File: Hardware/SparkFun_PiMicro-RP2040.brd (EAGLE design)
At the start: 17.8 x 33 mm, 105 parts, among them J2 Qwiic, J5 USB Female Type C Connector, U1 3.3V, U2 RP2040, U3 WS2812-2020, U4 W25QXX128MBIT, Y1 12MHz

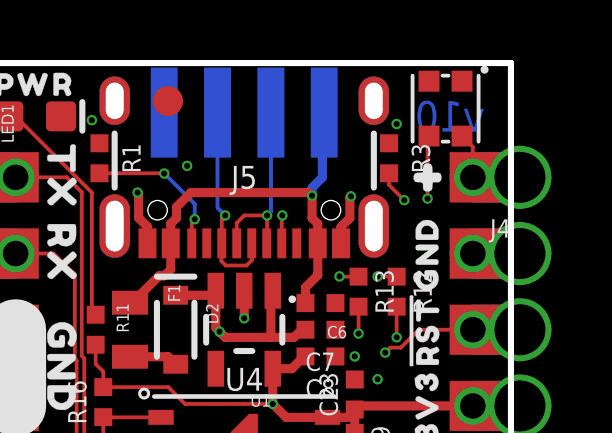
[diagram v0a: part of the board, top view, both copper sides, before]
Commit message: Increase 1.8V trace thickness. Fix reversed 3 silk.
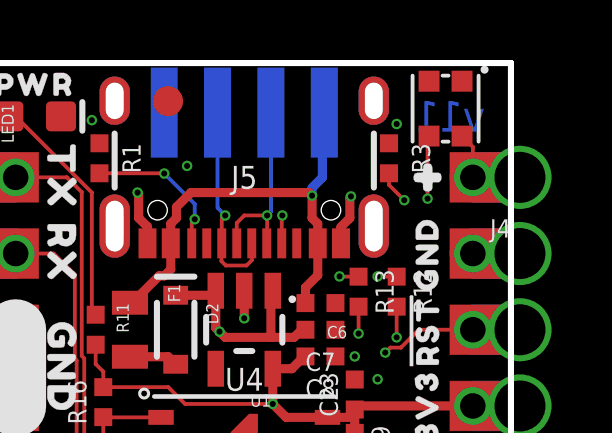
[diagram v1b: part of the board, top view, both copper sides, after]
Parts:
- moved U$15 1.02 mm to (15.0, 26.7), turned to 90 degrees
- moved U$19 0.13 mm to (3.17, 29.2)
- moved U$21 0.13 mm to (3.05, 26.7)
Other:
- board text added: "v11"
- board text removed: "v10"
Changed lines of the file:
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@@
 <?xml version="1.0" encoding="utf-8"?>
 <!DOCTYPE eagle SYSTEM "eagle.dtd">
-<eagle version="9.6.0">
+<eagle version="9.6.2">
 <drawing>
 <settings>
@@
 <layers>
 <layer number="1" name="Top" color="4" fill="1" visible="yes" active="yes"/>
-<layer number="2" name="GND/Vert" color="1" fill="3" visible="no" active="yes"/>
-<layer number="15" name="3.3V/Horz" color="4" fill="6" visible="no" active="yes"/>
+<layer number="2" name="GND/Vert" color="1" fill="3" visible="yes" active="yes"/>
+<layer number="15" name="3.3V/Horz" color="4" fill="6" visible="yes" active="yes"/>
 <layer number="16" name="Bottom" color="1" fill="1" visible="yes" active="yes"/>
 <layer number="17" name="Pads" color="2" fill="1" visible="yes" active="yes"/>
@@
 <layer number="44" name="Drills" color="7" fill="1" visible="no" active="yes"/>
 <layer number="45" name="Holes" color="7" fill="1" visible="yes" active="yes"/>
-<layer number="46" name="Milling" color="3" fill="1" visible="no" active="yes"/>
+<layer number="46" name="Milling" color="3" fill="1" visible="yes" active="yes"/>
 <layer number="47" name="Measures" color="7" fill="1" visible="no" active="yes"/>
 <layer number="48" name="Document" color="7" fill="1" visible="no" active="yes"/>
-<layer number="49" name="Reference" color="13" fill="1" visible="yes" active="yes"/>
+<layer number="49" name="Reference" color="13" fill="1" visible="no" active="yes"/>
 <layer number="50" name="dxf" color="7" fill="1" visible="no" active="yes"/>
 <layer number="51" name="tDocu" color="6" fill="1" visible="yes" active="yes"/>
@@
 <wire x1="17.78" y1="0" x2="17.78" y2="33.02" width="0.2032" layer="20"/>
 <wire x1="17.78" y1="33.02" x2="0" y2="33.02" width="0.2032" layer="20"/>
-<text x="15.748" y="31.242" size="1.016" layer="16" font="vector" ratio="25" rot="MR0" align="center">v10</text>
+<text x="15.748" y="31.242" size="1.016" layer="16" font="vector" ratio="25" rot="MR0" align="center">v11</text>
 <wire x1="1.27" y1="24.13" x2="1.27" y2="21.59" width="2.032" layer="21"/>
 <wire x1="1.27" y1="24.13" x2="1.27" y2="21.59" width="2.032" layer="22"/>
@@
 <element name="U$13" library="output" package="A21" value="" x="14.478" y="16.51" smashed="yes" rot="MR0"/>
 <element name="U$14" library="output" package="A32" value="" x="14.478" y="19.05" smashed="yes" rot="MR0"/>
-<element name="U$19" library="output" package="TX0" value="" x="3.302" y="29.21" smashed="yes" rot="MR0"/>
-<element name="U$21" library="output" package="RX1" value="" x="3.175" y="26.67" smashed="yes" rot="MR0"/>
+<element name="U$19" library="output" package="TX0" value="" x="3.175" y="29.21" smashed="yes" rot="MR0"/>
+<element name="U$21" library="output" package="RX1" value="" x="3.048" y="26.67" smashed="yes" rot="MR0"/>
 <element name="U$22" library="output" package="GND2" value="" x="2.921" y="22.86" smashed="yes" rot="MR270"/>
 <element name="U$23" library="output" package="20" value="" x="2.667" y="19.05" smashed="yes" rot="MR0"/>
@@
 <element name="U$34" library="output" package="#RST#0" value="" x="13.843" y="24.13" smashed="yes" rot="MR0"/>
 <element name="U$16" library="output" package="3V3_0" value="" x="13.716" y="21.59" smashed="yes" rot="MR0"/>
-<element name="U$15" library="output" package="GND2" value="" x="13.97" y="26.67" smashed="yes" rot="MR0"/>
+<element name="U$15" library="output" package="GND2" value="" x="14.986" y="26.67" smashed="yes" rot="MR90"/>
 <element name="U$18" library="output" package="PIMICRO0" value="" x="9.525" y="15.748" smashed="yes" rot="MR270"/>
 <element name="U$35" library="output" package="RP20400" value="" x="11.176" y="15.875" smashed="yes" rot="MR270"/>
@@
 <wire x1="9.271" y1="9.398" x2="9.017" y2="9.398" width="0.2032" layer="1"/>
 <via x="9.017" y="9.398" extent="1-16" drill="0.2"/>
-<wire x1="9.017" y1="9.398" x2="8.509" y2="9.906" width="0.127" layer="2"/>
-<wire x1="8.509" y1="13.462" x2="8.89" y2="13.843" width="0.127" layer="2"/>
-<wire x1="8.509" y1="13.462" x2="8.509" y2="9.906" width="0.127" layer="2"/>
+<wire x1="9.017" y1="9.398" x2="8.763" y2="9.398" width="0.2032" layer="2"/>
+<wire x1="8.763" y1="9.398" x2="8.382" y2="9.779" width="0.2032" layer="2"/>
+<wire x1="8.382" y1="13.335" x2="8.89" y2="13.843" width="0.2032" layer="2"/>
+<wire x1="8.382" y1="13.335" x2="8.382" y2="9.779" width="0.2032" layer="2"/>
 <via x="8.89" y="13.843" extent="1-16" drill="0.2"/>
 <wire x1="8.89" y1="13.843" x2="8.69" y2="14.043" width="0.2032" layer="1"/>

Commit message: Cleaning up schematic
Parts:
- removed FRAME1: FRAME-LETTER, SparkFun-Aesthetics:CREATIVE_COMMONS
- added FRAME2: FRAME-LEDGER, SparkFun-Aesthetics:CREATIVE_COMMONS
- R14: value 200OHM-0402T-1/16W-1% -> 200
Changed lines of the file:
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@@
 <attribute name="PROD_ID" value="CONN-14122" x="8.89" y="26.67" size="1.778" layer="27" rot="R180" display="off"/>
-</element>
-<element name="FRAME1" library="SparkFun-Aesthetics" package="CREATIVE_COMMONS" value="FRAME-LETTER" x="43.18" y="-15.24" smashed="yes">
-<attribute name="DESIGNER" value="" x="43.18" y="-15.24" size="1.778" layer="27" font="vector" ratio="15" display="off"/>
-<attribute name="REV" value="" x="43.18" y="-15.24" size="1.778" layer="27" font="vector" ratio="15" display="off"/>
 </element>
 <element name="LOGO5" library="SparkFun-Aesthetics" package="ORDERING_INSTRUCTIONS" value="SPECIAL_INSTRUCTIONS-ORDERING" x="22.86" y="50.8" smashed="yes"/>
@@
 <attribute name="VALUE" x="8.89" y="15.567" size="0.6096" layer="27" font="vector" ratio="20" align="top-center"/>
 </element>
-<element name="R14" library="SparkFun-Resistors" package="0402-TIGHT" value="200OHM-0402T-1/16W-1%" x="13.335" y="18.288" smashed="yes" rot="R270">
+<element name="R14" library="SparkFun-Resistors" package="0402-TIGHT" value="200" x="13.335" y="18.288" smashed="yes" rot="R270">
 <attribute name="NAME" x="13.897" y="18.288" size="0.6096" layer="25" font="vector" ratio="20" rot="R270" align="bottom-center"/>
 <attribute name="PROD_ID" value="RES-15550" x="-43.815" y="22.098" size="1.778" layer="27" font="vector" ratio="15" rot="R270" display="off"/>
@@
 <element name="U$37" library="output" package="R0" value="" x="12.3698" y="4.3942" smashed="yes"/>
 <element name="U$5" library="output" package="#0" value="" x="15.1" y="29.2" smashed="yes"/>
+<element name="FRAME2" library="SparkFun-Aesthetics" package="CREATIVE_COMMONS" value="FRAME-LEDGER" x="15.24" y="-24.13" smashed="yes">
+<attribute name="DESIGNER" value="" x="15.24" y="-24.13" size="1.778" layer="27" font="vector" ratio="15" display="off"/>
+<attribute name="REV" value="" x="15.24" y="-24.13" size="1.778" layer="27" font="vector" ratio="15" display="off"/>
+</element>
 </elements>
 <signals>

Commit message: Update silk. Adjust a few 0603 components.
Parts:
- removed U$18: (no value), output:PIMICRO0
- removed U$35: (no value), output:RP20400
- added U$38: (no value), output:RP20401
- added U$4: (no value), output:PRO_MICRO0
- moved U$37 1.94 mm to (14.0, 5.41)
- moved U$36 1.82 mm to (3.86, 5.16)
- moved U$19 0.40 mm to (2.79, 29.1), turned to 270 degrees
- moved R16 0.28 mm to (3.94, 21.6)
- moved C16 0.25 mm to (3.94, 14.6)
- moved R15 0.25 mm to (3.94, 19.6)
- moved U$21 0.25 mm to (2.79, 26.7), turned to 270 degrees
- turned U$15 to 270 degrees

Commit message: Silk update
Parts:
- moved LOGO5 27.9 mm to (-5.08, 50.8), flipped to the bottom
- moved J3 15.2 mm to (16.5, 1.27), flipped to the bottom
- moved J4 15.2 mm to (1.27, 29.2), flipped to the bottom
- moved U$73 14.0 mm to (15.9, 32.3), flipped to the bottom
- moved LED1 14.0 mm to (15.9, 31.2), flipped to the bottom
- moved U$3 13.7 mm to (15.7, 31.2), flipped to the top
- moved U3 13.4 mm to (2.18, 31.5), flipped to the bottom
- moved FRAME2 12.7 mm to (2.54, -24.1), flipped to the bottom
- moved U$23 12.4 mm to (15.1, 19.1), flipped to the top
- moved U$25 12.4 mm to (15.1, 14.0), flipped to the top
- moved U$26 12.4 mm to (15.1, 11.4), flipped to the top
- moved U$27 12.4 mm to (15.1, 9.02), flipped to the top
- moved U$6 12.4 mm to (15.1, 6.35), flipped to the top
- moved U$7 12.4 mm to (15.1, 3.81), flipped to the top
- moved U$8 12.4 mm to (15.1, 1.27), flipped to the top
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
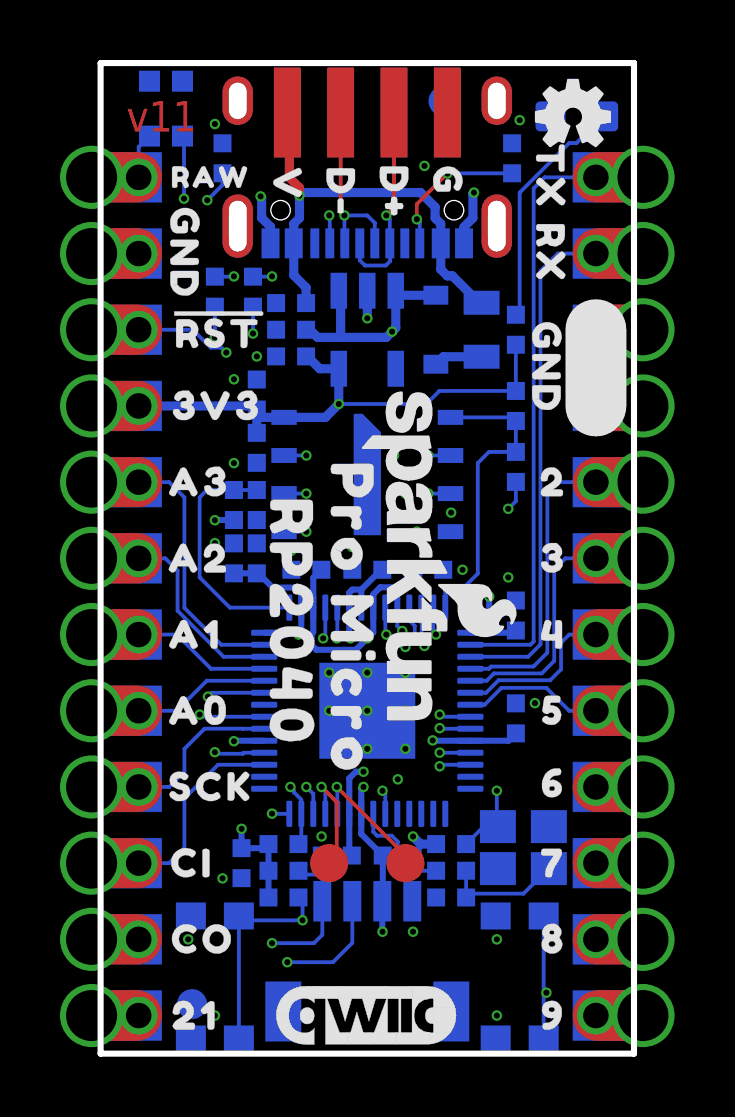
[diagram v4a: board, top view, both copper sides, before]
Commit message: Flip board to standard view
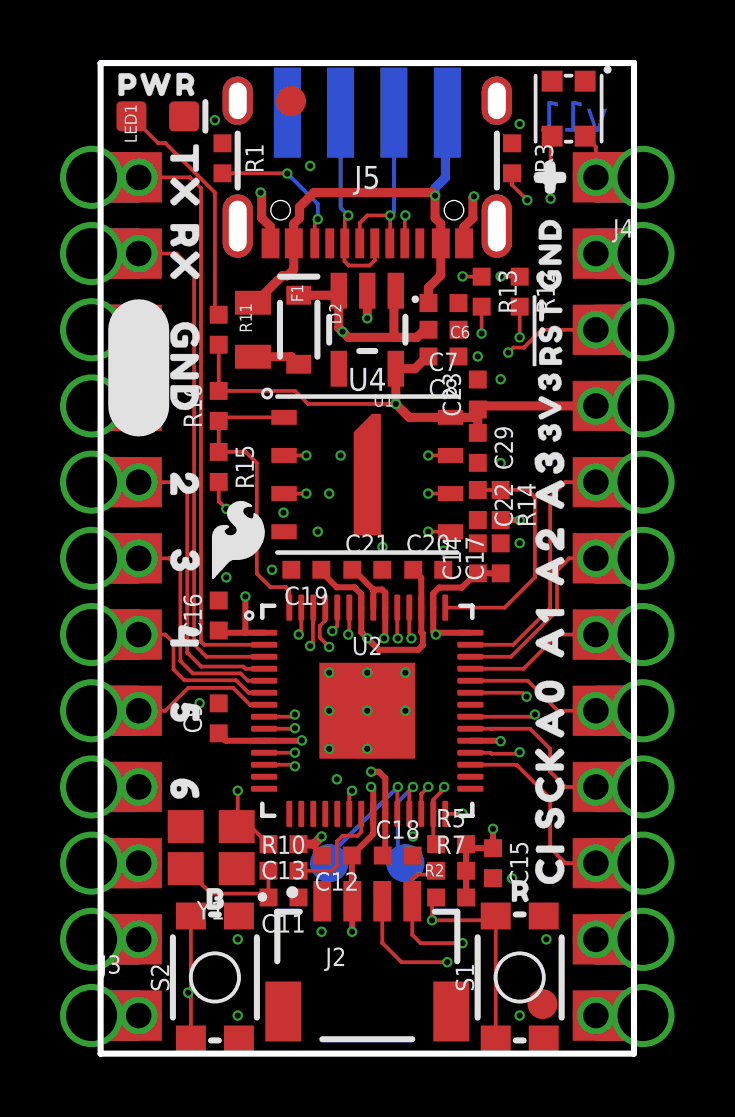
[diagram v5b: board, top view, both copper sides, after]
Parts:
- moved LOGO5 27.9 mm to (22.9, 50.8), flipped to the top
- moved J3 15.2 mm to (1.27, 1.27), flipped to the top
- moved J4 15.2 mm to (16.5, 29.2), flipped to the top
- moved U$73 14.0 mm to (1.90, 32.3), flipped to the top
- moved LED1 14.0 mm to (1.91, 31.2), flipped to the top
- moved U$3 13.7 mm to (2.03, 31.2), flipped to the bottom
- moved U3 13.4 mm to (15.6, 31.5), flipped to the top
- moved FRAME2 12.7 mm to (15.2, -24.1), flipped to the top
- moved U$23 12.4 mm to (2.67, 19.1), flipped to the bottom
- moved U$24 12.4 mm to (2.67, 16.5), flipped to the bottom
- moved U$25 12.4 mm to (2.67, 14.0), flipped to the bottom
- moved U$26 12.4 mm to (2.67, 11.4), flipped to the bottom
- moved U$27 12.4 mm to (2.67, 9.02), flipped to the bottom
- moved U$6 12.4 mm to (2.67, 6.35), flipped to the bottom
- moved U$7 12.4 mm to (2.67, 3.81), flipped to the bottom
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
